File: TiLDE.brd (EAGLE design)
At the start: 100 x 57 mm, 79 parts, among them IC1 L78M05CDT-TR, J1 Digital, J2 Analog, J4 POWER, Q1 CSM-3X-CRYSTALCSM-3X, U1 ATMEGA32U4-AU, U2 MCP73831, X1 USB-MICROB, X2 53048-02

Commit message: change usb, fix silk screen, add ucl logo
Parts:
- removed X1: USB-MICROB, SparkFun-Connectors:USB-MICROB
- added U$2: UCL-LOGO, TiLDA:UCL-LOGO
- added USB1: MICRO-USB-ZX62-B-5PA, serial:ZX62-B-5PA
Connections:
- net GND: now also USB1.5, USB1.GND@1, USB1.GND@2, USB1.GND@3, USB1.GND@4, USB1.GND@5, USB1.GND@6; no longer X1.GND
- net N$13: now also USB1.1; no longer X1.VBUS
- net N$2: now also USB1.2; no longer X1.D-
- net N$5: now also USB1.3; no longer X1.D+

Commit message: fix wireless MO and MI, remove un needed reset cap
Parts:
- removed C2: 0.1uF, resistor:C0603K
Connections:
- removed net RST: C2.1
- net MISO: now also JP5.7; no longer JP5.6
- net MOSI: now also JP5.6; no longer JP5.7
- net RESET: no longer C2.2
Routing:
- net MISO: track 65.8 -> 68.8 mm
- net MOSI: track 58.0 -> 60.5 mm, vias 1 -> 3
- net RESET: track 84.4 -> 83.5 mm

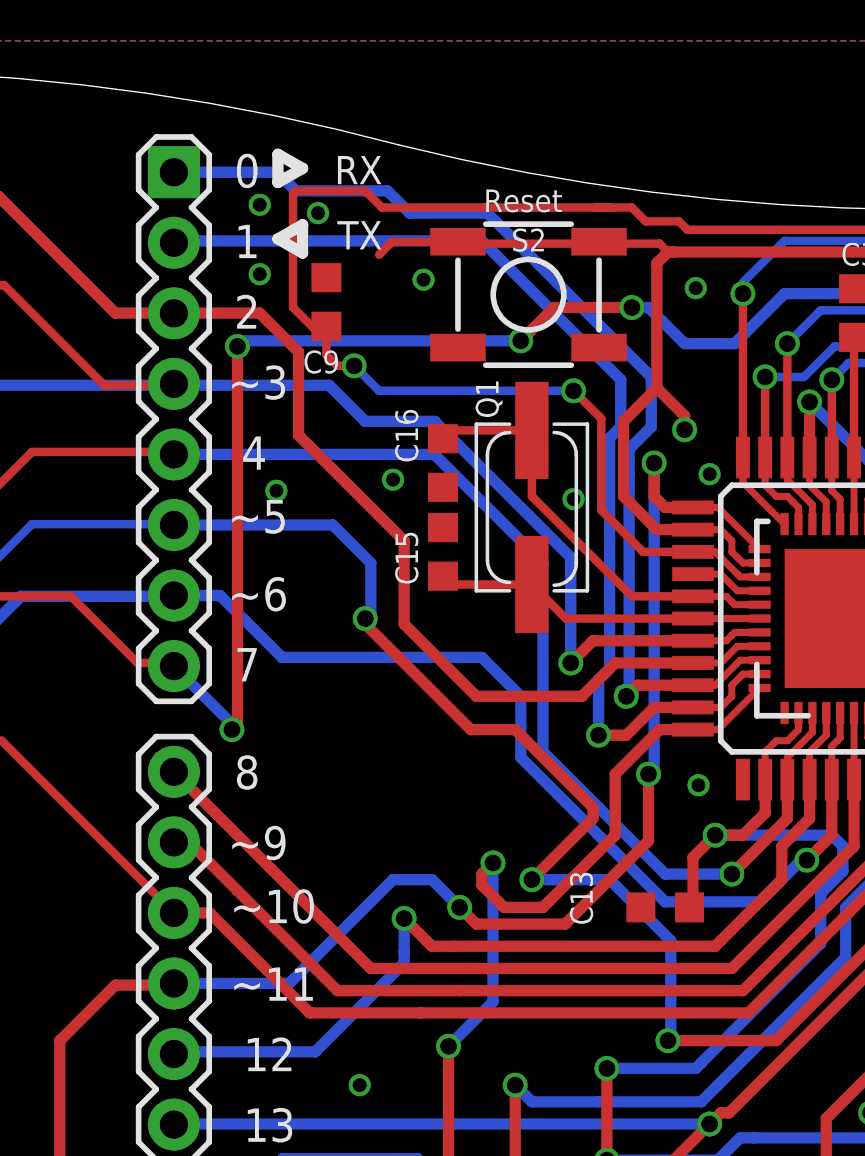
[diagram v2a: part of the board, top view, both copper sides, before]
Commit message: Fix routing under crystal
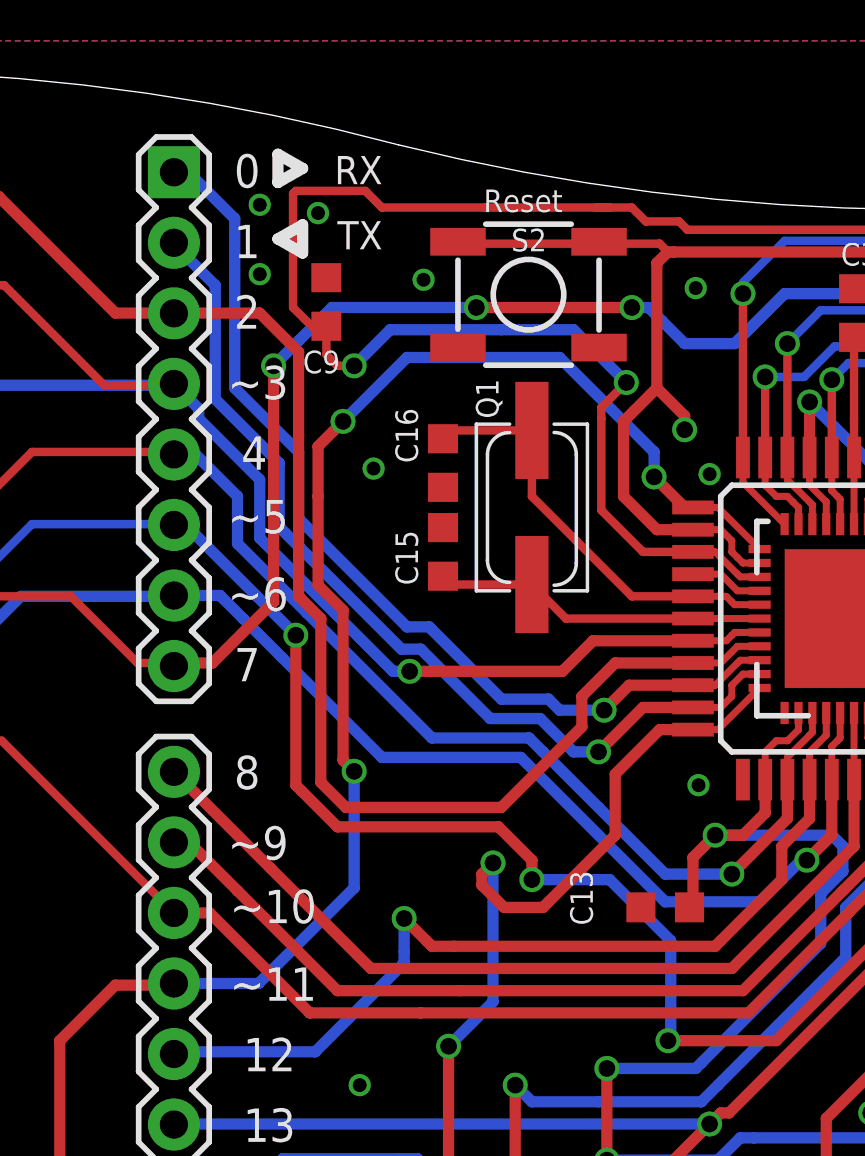
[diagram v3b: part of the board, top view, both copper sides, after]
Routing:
- net D2/SDA: track 143.0 -> 152.1 mm
- net D11: track 59.1 -> 64.1 mm
- net D7: track 68.5 -> 63.8 mm, vias 5 -> 4
- net TX-O: track 38.3 -> 34.0 mm
- net VCC: track 253.9 -> 257.0 mm
- net RESET: track 83.5 -> 80.5 mm
- net D4: track 49.2 -> 46.3 mm
- net RX-I: track 37.7 -> 34.8 mm
- net D5: track 71.3 -> 68.6 mm
- net D6: track 47.1 -> 45.8 mm
- net GND: vias 35 -> 33
